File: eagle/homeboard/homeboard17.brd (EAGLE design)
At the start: 100 x 80 mm, 119 parts, among them IC1 XCF02S, IC2 25LC080SN, IC3 ATMEGA32U2-TQFP, Q5 BC848SMD, Q6 BC848SMD, Q7 BC848SMD, Q8 BC848SMD, T1 BSS138, T2 BC848, T3 BSS138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

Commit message: mah
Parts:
- moved U$2 56.7 mm to (15.9, 63.9), turned to 270 degrees
- moved X1 32.5 mm to (21.5, 77.0)
- moved X4 8.50 mm to (42.5, 68.2)
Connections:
- net CLK16: now also U1.P125
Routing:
- net CLK16: track 0.00 -> 29.8 mm
- net VCC: track 383.0 -> 393.9 mm, vias 23 -> 24
- net GND: track 787.4 -> 791.3 mm, vias 32 -> 33

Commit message: closer and closer
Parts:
- moved IC2 16.5 mm to (50.1, 34.9)
- moved X5 1.58 mm to (93.5, 64.5)
- moved X6 1.00 mm to (65.8, 69.8)
- moved IC3 0.56 mm to (57.5, 40.0)
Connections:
- new net FPGA_RESET: IC3.22, U1.P124
- net TCK: now also IC3.19; no longer IC3.18
- net TDO_EXP: now also IC3.23; no longer IC3.22
- net TMS: now also IC3.18; no longer IC3.19
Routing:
- net GND: track 791.3 -> 703.4 mm
- net FPGA_RESET: track 0.00 -> 46.3 mm, vias 0 -> 2
- net TDO_FPGA: track 2.21 -> 37.7 mm, vias 0 -> 2
- net N$40: track 30.7 -> 59.7 mm, vias 1 -> 2
- net TDI_FPGA: track 23.0 -> 51.3 mm, vias 0 -> 1
- net TDO_PROM: track 0.00 -> 9.32 mm
- net N$49: track 0.00 -> 7.66 mm
- net N$68: track 0.00 -> 6.33 mm
- net TCK: track 8.83 -> 11.2 mm
- net TMS: track 7.83 -> 9.97 mm

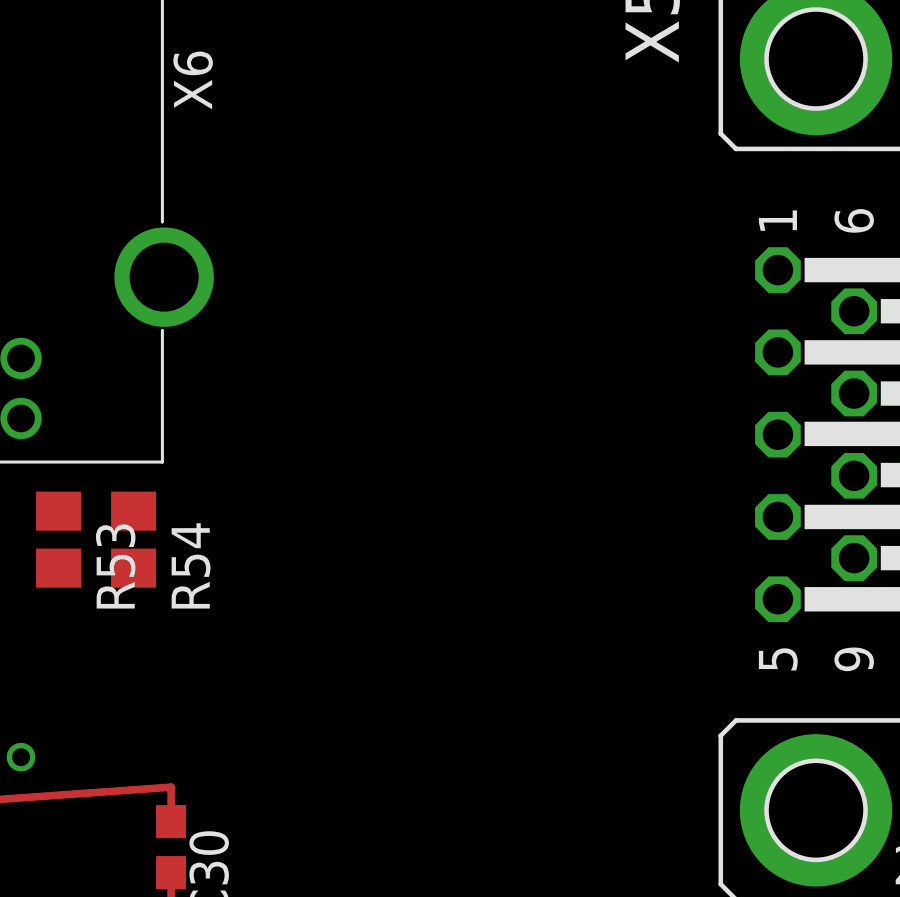
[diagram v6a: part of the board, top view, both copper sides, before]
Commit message: adding xtal to atmega
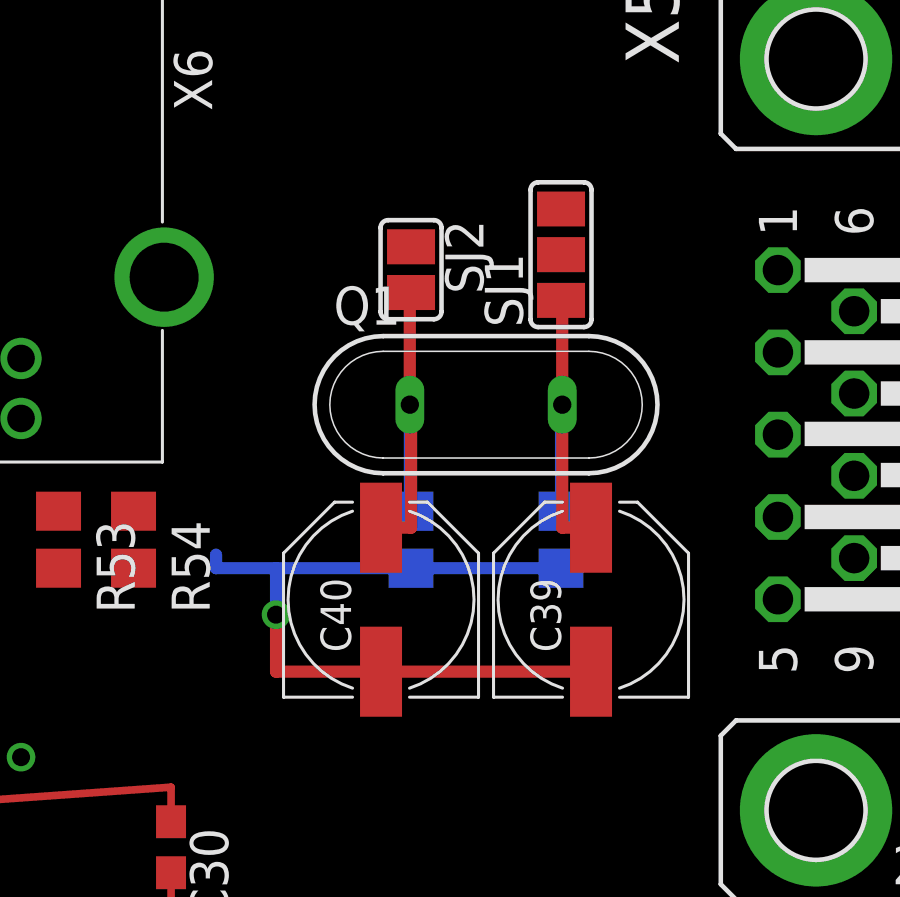
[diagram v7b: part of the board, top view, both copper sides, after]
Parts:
- added C37, C38: (no value), rcl:C0805
- added C39, C40: 100u, rcl:PANASONIC_D
- added Q1: (no value), special:QS
- added SJ1: (no value), jumper:SJ_2
- added SJ2: (no value), jumper:SJ
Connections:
- new net EXTCLK: SJ1.3
- new net N$10: IC3.2, SJ2.1
- new net N$12: C37.2, C40.+, Q1.1, SJ2.2
- new net N$14: C38.2, C39.+, Q1.2, SJ1.1
- new net N$9: IC3.1, SJ1.2
- net GND: now also C37.1, C38.1, C39.-, C40.-
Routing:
- net GND: track 703.4 -> 729.4 mm, vias 33 -> 34
- net N$12: track 0.00 -> 12.5 mm
- net N$14: track 0.00 -> 12.1 mm
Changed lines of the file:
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@@
 <setting verticaltext="up"/>
 </settings>
-<grid distance="0.5" unitdist="mm" unit="mm" style="lines" multiple="1" display="no" altdistance="0.25" altunitdist="mm" altunit="mm"/>
+<grid distance="0.5" unitdist="mm" unit="mm" style="lines" multiple="1" display="yes" altdistance="0.25" altunitdist="mm" altunit="mm"/>
 <layers>
 <layer number="1" name="Top" color="4" fill="1" visible="yes" active="yes"/>
@@
 <attribute name="OC_FARNELL" value="unknown" x="24" y="24.5" size="1.778" layer="27" display="off"/>
 </element>
+<element name="Q1" library="special" package="QS" value="" x="82.5" y="65.5"/>
+<element name="SJ1" library="jumper" package="SJ_2" value="" x="85" y="70.5" rot="R90"/>
+<element name="SJ2" library="jumper" package="SJ" value="" x="80" y="70" rot="R270"/>
+<element name="C37" library="rcl" package="C0805" value="" x="80" y="61" rot="MR90"/>
+<element name="C38" library="rcl" package="C0805" value="" x="85" y="61" rot="MR90"/>
+<element name="C39" library="rcl" package="PANASONIC_D" value="100u" x="86" y="59" rot="R90"/>
+<element name="C40" library="rcl" package="PANASONIC_D" value="100u" x="79" y="59" rot="R90"/>
 </elements>
 <signals>
@@
 <wire x1="14.5" y1="61" x2="14.5" y2="59.5" width="0.254" layer="16"/>
 <wire x1="14.5" y1="59.5" x2="15" y2="59" width="0.254" layer="16"/>
+<contactref element="C38" pad="1"/>
+<contactref element="C39" pad="-"/>
+<contactref element="C40" pad="-"/>
+<contactref element="C37" pad="1"/>
+<wire x1="85" y1="60.05" x2="80" y2="60.05" width="0.4064" layer="16"/>
+<wire x1="80" y1="60.05" x2="75.5" y2="60.05" width="0.4064" layer="16"/>
+<wire x1="75.5" y1="60.05" x2="73.5" y2="60.05" width="0.4064" layer="16"/>
+<wire x1="73.5" y1="60.05" x2="73.5" y2="60.5" width="0.4064" layer="16"/>
+<wire x1="79" y1="56.6" x2="86" y2="56.6" width="0.4064" layer="1"/>
+<wire x1="86" y1="56.6" x2="86" y2="56.5" width="0.4064" layer="1"/>
+<wire x1="79" y1="56.6" x2="75.5" y2="56.6" width="0.4064" layer="1"/>
+<wire x1="75.5" y1="56.6" x2="75.5" y2="58.5" width="0.4064" layer="1"/>
+<via x="75.5" y="58.5" extent="1-16" drill="0.6" shape="square"/>
+<wire x1="75.5" y1="58.5" x2="75.5" y2="60.05" width="0.4064" layer="16"/>
 <wire x1="94.77" y1="63.1284" x2="93.5" y2="77.0222" width="0" layer="19" extent="1-1"/>
-<wire x1="88.35" y1="45.5" x2="94.77" y2="63.1284" width="0" layer="19" extent="1-1"/>
-<wire x1="88.35" y1="40.5" x2="88.35" y2="45.5" width="0" layer="19" extent="1-1"/>
-<wire x1="88.35" y1="35.5" x2="88.35" y2="40.5" width="0" layer="19" extent="1-1"/>
-<wire x1="88.85" y1="31.5" x2="88.35" y2="35.5" width="0" layer="19" extent="1-1"/>
-<wire x1="82.5" y1="30.25" x2="88.85" y2="31.5" width="0" layer="19" extent="1-1"/>
-<wire x1="82.5" y1="28.75" x2="82.5" y2="30.25" width="0" layer="19" extent="1-1"/>
-<wire x1="77.75" y1="25.5" x2="82.5" y2="28.75" width="0" layer="19" extent="1-1"/>
-<wire x1="74" y1="30.75" x2="77.75" y2="25.5" width="0" layer="19" extent="16-16"/>
+<wire x1="85" y1="60.05" x2="94.77" y2="63.1284" width="0" layer="19" extent="16-16"/>
+<wire x1="72" y1="49.9" x2="75.5" y2="56.6" width="0" layer="19" extent="1-1"/>
 <wire x1="59.393396875" y1="24.737409375" x2="59.5" y2="20" width="0" layer="19" extent="1-16"/>
 <wire x1="67" y1="53.75" x2="72" y2="49.9" width="0" layer="19" extent="1-1"/>
-<wire x1="48.198553125" y1="37.4890875" x2="60.75" y2="32.25" width="0" layer="19" extent="1-16"/>
+<wire x1="77.75" y1="25.5" x2="74" y2="30.75" width="0" layer="19" extent="16-16"/>
+<wire x1="82.5" y1="28.75" x2="77.75" y2="25.5" width="0" layer="19" extent="1-1"/>
+<wire x1="82.5" y1="30.25" x2="82.5" y2="28.75" width="0" layer="19" extent="1-1"/>
+<wire x1="88.85" y1="31.5" x2="82.5" y2="30.25" width="0" layer="19" extent="1-1"/>
+<wire x1="88.35" y1="35.5" x2="88.85" y2="31.5" width="0" layer="19" extent="1-1"/>
+<wire x1="88.35" y1="40.5" x2="88.35" y2="35.5" width="0" layer="19" extent="1-1"/>
+<wire x1="88.35" y1="45.5" x2="88.35" y2="40.5" width="0" layer="19" extent="1-1"/>
 <wire x1="56.5" y1="8.5" x2="56.1" y2="17" width="0" layer="19" extent="1-16"/>
 <wire x1="15" y1="59" x2="15.11" y2="59" width="0" layer="19" extent="16-16"/>
@@
 <wire x1="41.97" y1="51.7" x2="42" y2="51.75" width="0" layer="19" extent="1-1"/>
 <wire x1="29.47" y1="51.7" x2="29.5" y2="51.75" width="0" layer="19" extent="1-1"/>
+<wire x1="48.198553125" y1="37.4890875" x2="49" y2="36.25" width="0" layer="19" extent="1-16"/>
 <wire x1="51" y1="57.75" x2="48" y2="56.5" width="0" layer="19" extent="16-16"/>
 <wire x1="19.2" y1="66.75" x2="24" y2="64" width="0" layer="19" extent="16-16"/>
 <wire x1="29.9778" y1="68.25" x2="27.5" y2="62" width="0" layer="19" extent="16-16"/>
 <wire x1="43.8716" y1="69.52" x2="41.5" y2="62" width="0" layer="19" extent="16-16"/>
-<wire x1="58.7" y1="44.2926" x2="48.198553125" y2="37.4890875" width="0" layer="19" extent="1-1"/>
+<wire x1="58.7" y1="44.2926" x2="50" y2="45.75" width="0" layer="19" extent="1-16"/>
 <wire x1="66.57" y1="1.73" x2="55.5" y2="5" width="0" layer="19" extent="1-1"/>
 <wire x1="84.5" y1="16.1" x2="77.75" y2="25.5" width="0" layer="19" extent="1-1"/>
@@
 <wire x1="12.57" y1="24.5" x2="12.5" y2="24.47" width="0" layer="19" extent="1-1"/>
 <wire x1="14" y1="31.25" x2="12.57" y2="24.5" width="0" layer="19" extent="16-16"/>
-<wire x1="59.393396875" y1="29.287409375" x2="63.5" y2="21.5" width="0" layer="19" extent="1-1"/>
-<wire x1="52.008553125" y1="32.2890875" x2="71.5" y2="30.4" width="0" layer="19" extent="1-1"/>
+<wire x1="52.008553125" y1="32.2890875" x2="46.42" y2="33.25" width="0" layer="19" extent="1-1"/>
+<wire x1="59.393396875" y1="30.643396875" x2="52.008553125" y2="32.2890875" width="0" layer="19" extent="1-1"/>
 <wire x1="61.7926" y1="42.8" x2="65" y2="52.25" width="0" layer="19" extent="1-1"/>
 <wire x1="61.7926" y1="42" x2="61.7926" y2="42.8" width="0" layer="19" extent="1-1"/>
@@
 <wire x1="37" y1="53" x2="57" y2="53" width="0.254" layer="16"/>
 </signal>
+<signal name="N$9">
+<contactref element="IC3" pad="1"/>
+<contactref element="SJ1" pad="2"/>
+<wire x1="60.3" y1="44.2926" x2="85" y2="70.5" width="0" layer="19" extent="1-1"/>
+</signal>
+<signal name="N$10">
+<contactref element="IC3" pad="2"/>
+<contactref element="SJ2" pad="1"/>
+<wire x1="59.5" y1="44.2926" x2="80" y2="70.762" width="0" layer="19" extent="1-1"/>
+</signal>
+<signal name="EXTCLK">
+<contactref element="SJ1" pad="3"/>
+</signal>
+<signal name="N$12">
+<contactref element="C37" pad="2"/>
+<contactref element="C40" pad="+"/>
+<contactref element="SJ2" pad="2"/>
+<contactref element="Q1" pad="1"/>
+<wire x1="80" y1="61.95" x2="79.96" y2="61.95" width="0.4064" layer="16"/>
+<wire x1="79.96" y1="61.95" x2="79.96" y2="65.5" width="0.4064" layer="16"/>
+<wire x1="80" y1="65.5" x2="80" y2="69.238" width="0" layer="19" extent="1-16"/>
+<wire x1="80" y1="69.238" x2="79.96" y2="69.238" width="0.4064" layer="1"/>
+<wire x1="79.96" y1="69.238" x2="79.96" y2="65.5" width="0.4064" layer="1"/>
+<wire x1="79" y1="61.4" x2="80" y2="61.4" width="0.4064" layer="1"/>
+<wire x1="80" y1="61.4" x2="80" y2="65.5" width="0.4064" layer="1"/>
+</signal>
+<signal name="N$14">
+<contactref element="Q1" pad="2"/>
+<contactref element="SJ1" pad="1"/>
+<contactref element="C39" pad="+"/>
+<contactref element="C38" pad="2"/>
+<wire x1="85" y1="61.95" x2="85" y2="65.5" width="0.4064" layer="16"/>
+<wire x1="85" y1="68.976" x2="85.04" y2="68.976" width="0.4064" layer="1"/>
+<wire x1="85.04" y1="68.976" x2="85.04" y2="65.5" width="0.4064" layer="1"/>
+<wire x1="86" y1="61.4" x2="85.04" y2="61.4" width="0.4064" layer="1"/>
+<wire x1="85.04" y1="61.4" x2="85.04" y2="65.5" width="0.4064" layer="1"/>
+<wire x1="85.04" y1="65.5" x2="85" y2="65.5" width="0" layer="19" extent="16-16"/>
+</signal>
 </signals>
